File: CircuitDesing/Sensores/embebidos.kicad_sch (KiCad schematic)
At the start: 0 parts

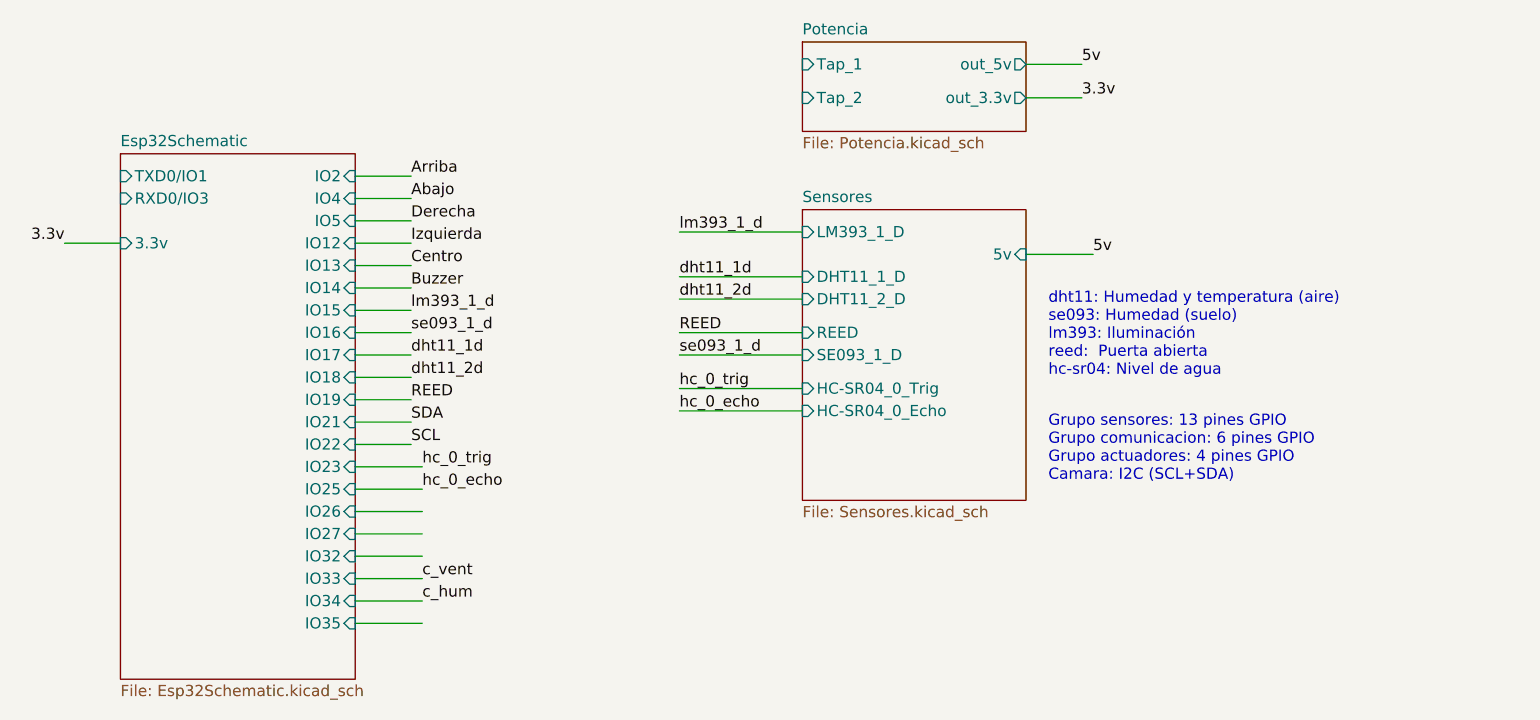
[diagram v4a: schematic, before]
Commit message: Modificaciones generales
Modificaciones a esquemático,  interacción con otros grupos, sistema de potencia.
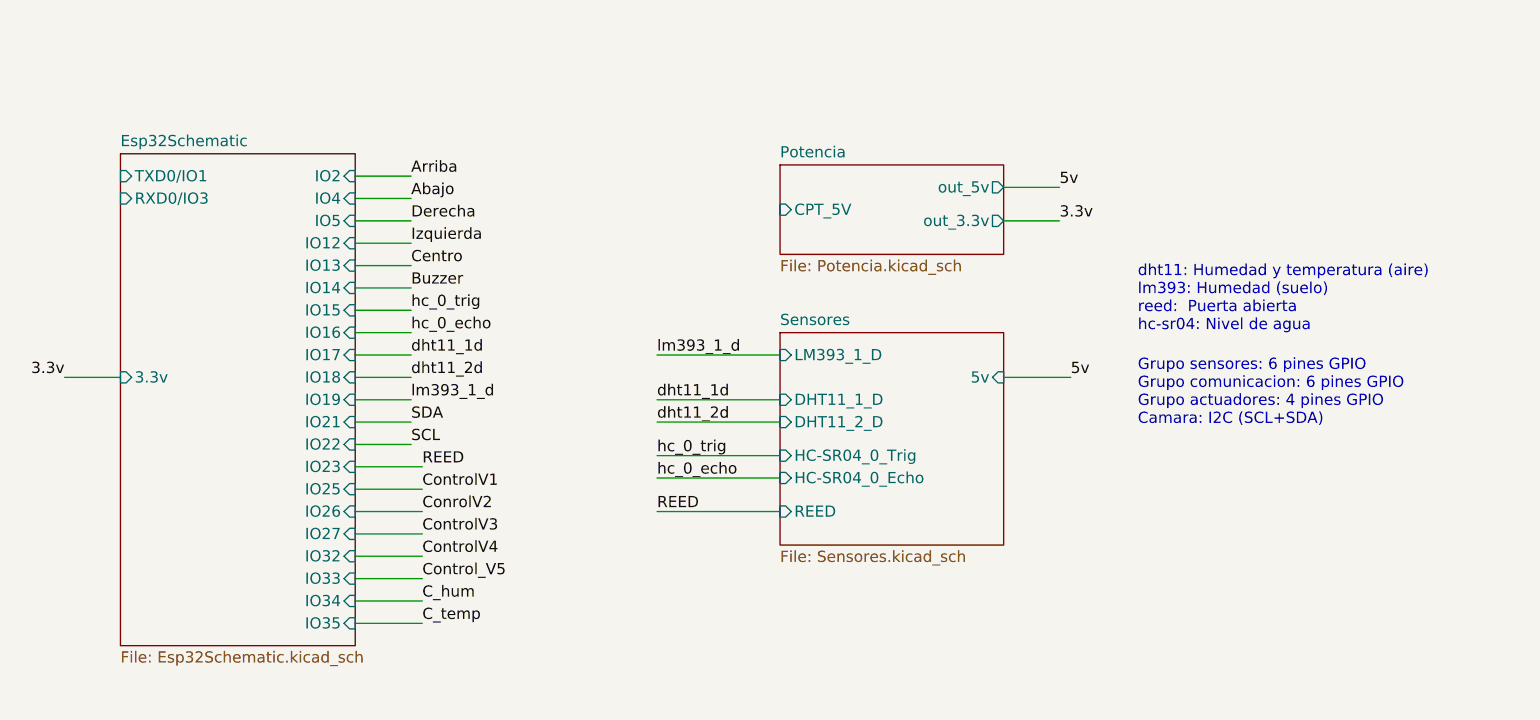
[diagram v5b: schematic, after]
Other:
- sheet Potencia ports: added CPT_5V; removed Tap_1, Tap_2
- sheet Sensores ports: added none; removed SE093_1_D
- note added: "Grupo sensores: 6 pines GPIO Grupo comunicacion: 6 pines GPIO Grupo actuadores: 4 pines GPIO Camara: I2C (SCL+SDA)"
- note added: "dht11: Humedad y temperatura (aire) lm393: Humedad (suelo) reed: Puerta abierta hc-sr04: Nivel de agua"
- note removed: "Grupo sensores: 13 pines GPIO Grupo comunicacion: 6 pines GPIO Grupo actuadores: 4 pines GPIO Camara: I2C (SCL+SDA)"
- note removed: "dht11: Humedad y temperatura (aire) se093: Humedad (suelo) lm393: Iluminación reed: Puerta abierta hc-sr04: Nivel de agua"

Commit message: Huellas
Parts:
- added HMI1: Conn_01x07, Connector_JST:JST_EH_B7B-EH-A_1x07_P2.50mm_Vertical, symbol Connector_Generic:Conn_01x07
- added I2C1, VENTILACION1: Conn_01x03, Connector_JST:JST_EH_B3B-EH-A_1x03_P2.50mm_Vertical, symbol Connector_Generic:Conn_01x03
- added RIEGO1: Conn_01x06, Connector_JST:JST_EH_B6B-EH-A_1x06_P2.50mm_Vertical, symbol Connector_Generic:Conn_01x06
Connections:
- net Abajo: now also HMI1.5 (Pin_5)
- net Arriba: now also HMI1.6 (Pin_6)
- net Buzzer: now also HMI1.1 (Pin_1)
- net C_hum: now also VENTILACION1.2 (Pin_2)
- net C_temp: now also VENTILACION1.1 (Pin_1)
- net Centro: now also HMI1.2 (Pin_2)
- net ConrolV2: now also RIEGO1.4 (Pin_4)
- net ControlV1: now also RIEGO1.5 (Pin_5)
- net ControlV3: now also RIEGO1.3 (Pin_3)
- net ControlV4: now also RIEGO1.2 (Pin_2)
- net Control_V5: now also RIEGO1.1 (Pin_1)
- net Derecha: now also HMI1.4 (Pin_4)
- net Izquierda: now also HMI1.3 (Pin_3)
- net SCL: now also I2C1.1 (Pin_1)
- net SDA: now also I2C1.2 (Pin_2)
- new net GND: HMI1.7 (Pin_7), I2C1.3 (Pin_3), RIEGO1.6 (Pin_6), VENTILACION1.3 (Pin_3)

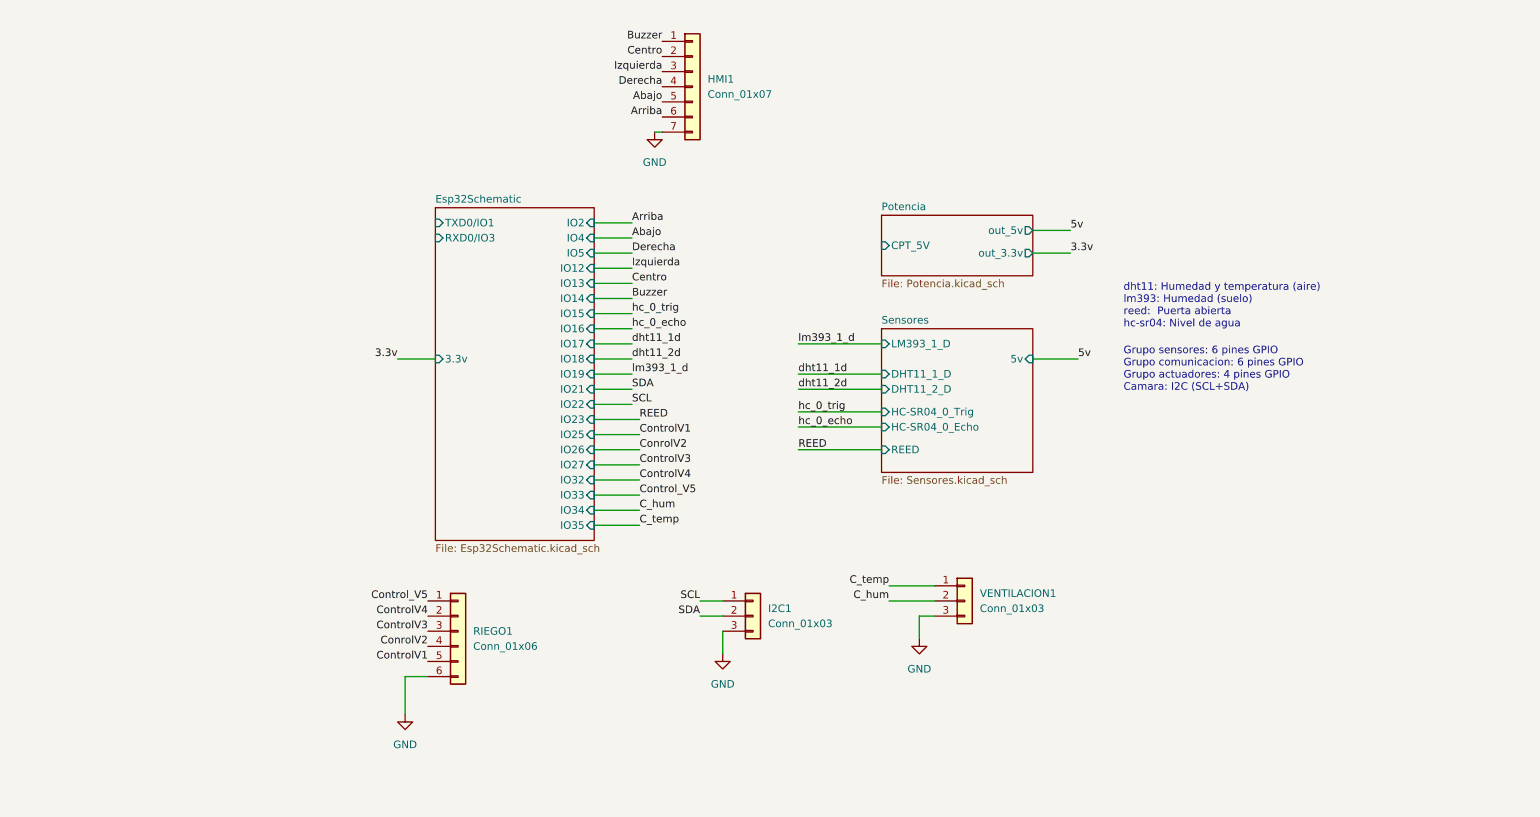
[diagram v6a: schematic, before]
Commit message: Listo para Ruteo
Cambios en programador, led usuario, pines 34 35 (solo entrada)
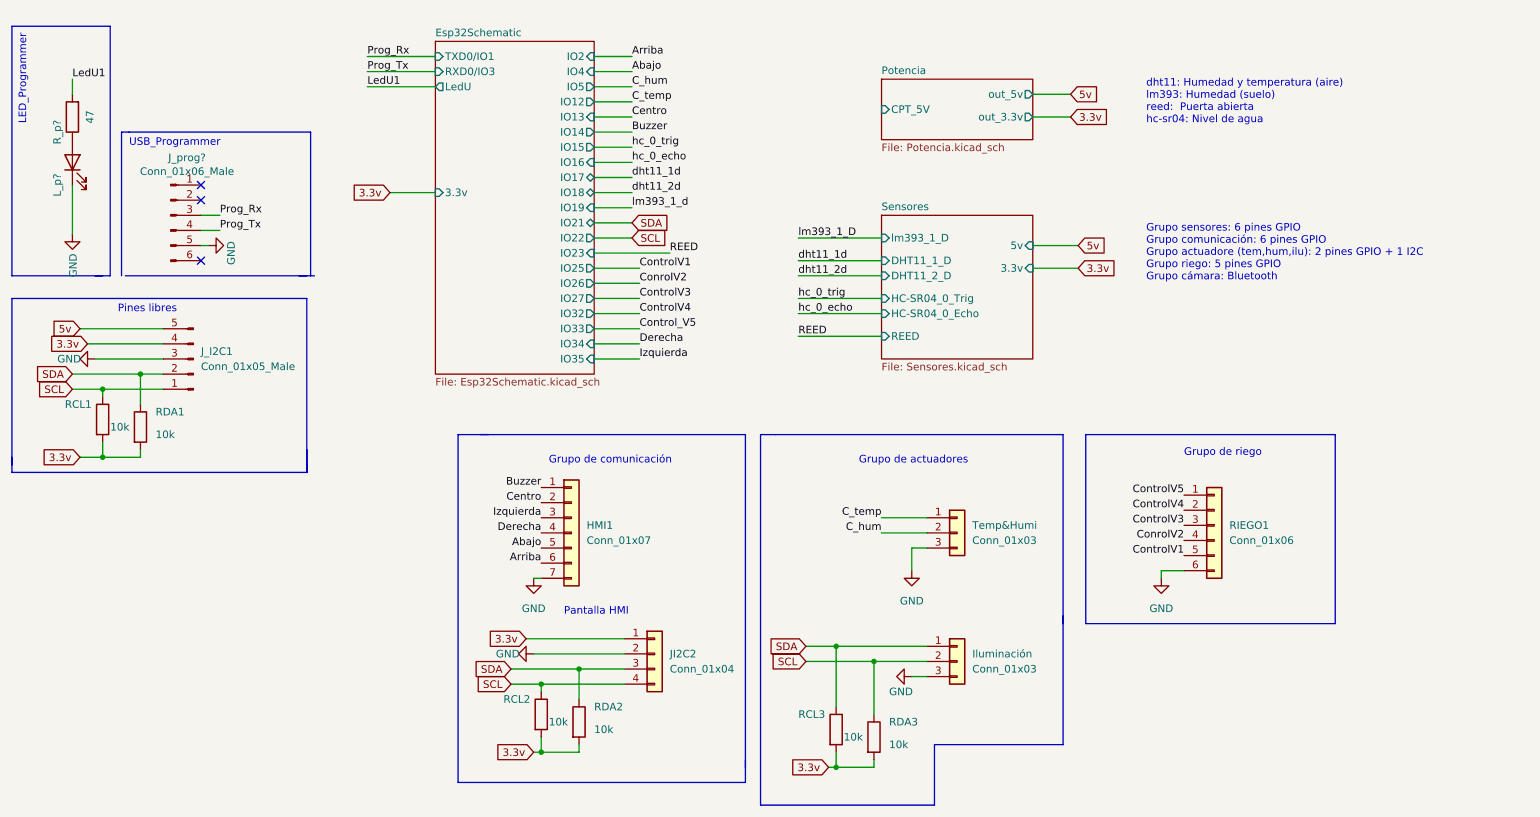
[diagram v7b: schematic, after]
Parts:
- removed I2C1: Conn_01x03, Connector_JST:JST_EH_B3B-EH-A_1x03_P2.50mm_Vertical, symbol Connector_Generic:Conn_01x03
- added Iluminación: Conn_01x03, Connector_JST:JST_EH_B3B-EH-A_1x03_P2.50mm_Vertical, symbol Connector_Generic:Conn_01x03
- added JI2C2: Conn_01x04, symbol Connector_Generic:Conn_01x04
- added J_I2C1: Conn_01x05_Male, Connector_PinSocket_2.54mm:PinSocket_1x05_P2.54mm_Horizontal, symbol Connector:Conn_01x05_Male
- added J_prog?: Conn_01x06_Male, Connector_PinHeader_2.54mm:PinHeader_1x06_P2.54mm_Horizontal, symbol Connector:Conn_01x06_Male
- added L_p?: LED, LED_SMD:LED_0805_2012Metric_Pad1.15x1.40mm_HandSolder, symbol Device:LED
- added RCL1, RCL2, RCL3, RDA1, RDA2, RDA3: 10k, Resistor_SMD:R_0805_2012Metric_Pad1.20x1.40mm_HandSolder, symbol Device:R
- added R_p?: 47, Resistor_SMD:R_0805_2012Metric_Pad1.20x1.40mm_HandSolder, symbol Device:R
- renumbered VENTILACION1 to Temp&Humi
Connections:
- net 3.3v: now also JI2C2.1 (Pin_1), J_I2C1.4 (Pin_4), RCL1.2, RCL2.2, RCL3.2, RDA1.2, RDA2.2, RDA3.2
- net 5v: now also J_I2C1.5 (Pin_5)
- net Control_V5: no longer RIEGO1.1 (Pin_1)
- net GND: now also Iluminación.3 (Pin_3), JI2C2.2 (Pin_2), J_I2C1.3 (Pin_3), J_prog?.5 (Pin_5), L_p?.1 (K)
- net SCL: now also Iluminación.2 (Pin_2), JI2C2.4 (Pin_4), J_I2C1.1 (Pin_1), RCL1.1, RCL2.1, RDA3.1
- net SDA: now also Iluminación.1 (Pin_1), JI2C2.3 (Pin_3), J_I2C1.2 (Pin_2), RCL3.1, RDA1.1, RDA2.1
- new net: L_p?.2 (A), R_p?.1
- new net ControlV5: RIEGO1.1 (Pin_1)
- new net LedU1: R_p?.2
- new net Prog_Rx: J_prog?.3 (Pin_3)
- new net Prog_Tx: J_prog?.4 (Pin_4)
- no-connect marks 0 -> 3
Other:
- sheet Esp32Schematic ports: added LedU; removed none
- sheet Sensores ports: added 3.3v, lm393_1_D; removed LM393_1_D
- note added: "Grupo de actuadores"
- note added: "Grupo de comunicación"
- note added: "Grupo de riego"
- note added: "Grupo sensores: 6 pines GPIO Grupo comunicación: 6 pines GPIO Grupo actuadore (tem,hum,ilu): 2 pines GPIO + 1 I2C Grupo riego: 5 pines GPIO Grupo cámara: Bluetooth"
- note added: "LED_Programmer"
- note added: "Pantalla HMI"
- note added: "Pines libres"
- note added: "USB_Programmer"
- note removed: "Grupo sensores: 6 pines GPIO Grupo comunicacion: 6 pines GPIO Grupo actuadores: 4 pines GPIO Camara: I2C (SCL+SDA)"
- moved on the sheet: HMI1, RIEGO1, Temp&Humi
